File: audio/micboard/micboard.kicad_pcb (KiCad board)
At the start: 2 copper layers, 11 x 7.5 mm, 4 parts, among them P1 CONN_01X04, U1 MIC

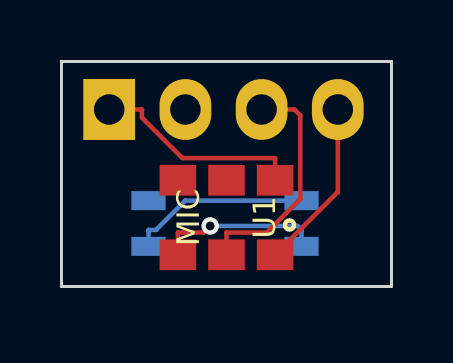
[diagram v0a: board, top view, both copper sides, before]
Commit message: correcting audio board vias
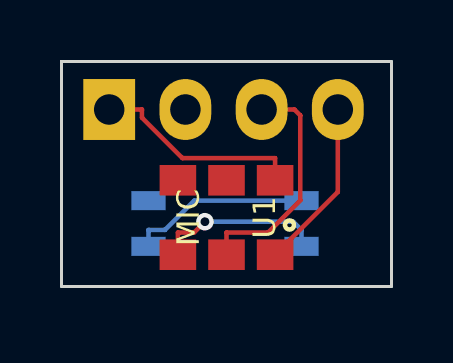
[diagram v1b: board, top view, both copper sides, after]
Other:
- net class Default: via_dia 0.5842 -> 0.635; via_drill 0.3302 -> 0.381
- rule via_min_drill: 0.3302 -> 0.381
- rule via_min_size: 0.5842 -> 0.635
- board text removed: "OUT GN - +"
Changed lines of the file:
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@@
     (links 7)
     (no_connects 0)
-    (area 148.949999 106.949999 160.050001 114.550001)
+    (area 148.007667 106.949999 160.792334 114.550001)
     (thickness 1.6)
-    (drawings 6)
+    (drawings 5)
     (tracks 24)
     (zones 0)
@@
     (segment_width 0.2)
     (edge_width 0.1)
-    (via_size 0.5842)
-    (via_drill 0.3302)
-    (via_min_size 0.5842)
-    (via_min_drill 0.3302)
+    (via_size 0.635)
+    (via_drill 0.381)
+    (via_min_size 0.635)
+    (via_min_drill 0.381)
     (uvia_size 0.508)
     (uvia_drill 0.127)
@@
     (visible_elements FFFFFF7F)
     (pcbplotparams
-      (layerselection 0x00030_80000001)
-      (usegerberextensions false)
+      (layerselection 0x010fc_80000001)
+      (usegerberextensions true)
       (excludeedgelayer true)
       (linewidth 0.100000)
@@
       (psa4output false)
       (plotreference true)
-      (plotvalue true)
+      (plotvalue false)
       (plotinvisibletext false)
       (padsonsilk false)
@@
       (outputformat 1)
       (mirror false)
-      (drillshape 1)
+      (drillshape 0)
       (scaleselection 1)
-      (outputdirectory ""))
+      (outputdirectory gerber/))
   )
   (net 0 "")
@@
     (clearance 0.1524)
     (trace_width 0.1524)
-    (via_dia 0.5842)
-    (via_drill 0.3302)
+    (via_dia 0.635)
+    (via_drill 0.381)
     (uvia_dia 0.508)
     (uvia_drill 0.127)
@@
       (net 3 +5V))
   )
-  (gr_text "OUT GN  -   +" (at 154.6 110.5) (layer B.SilkS)
-    (effects (font (size 0.75 0.75) (thickness 0.1875)) (justify mirror))
-  )
   (gr_line (start 149 114.5) (end 149 107) (angle 90) (layer Edge.Cuts) (width 0.1))
   (gr_line (start 160 114.5) (end 149 114.5) (angle 90) (layer Edge.Cuts) (width 0.1))
@@
   (gr_line (start 149 107) (end 160 107) (angle 90) (layer Edge.Cuts) (width 0.1))
   (gr_line (start 149 107) (end 149 107.1) (angle 90) (layer Edge.Cuts) (width 0.1))
-  (via (at 153.9569 112.4816) (size 0.5842) (layers F.Cu B.Cu) (net 1))
-  (segment (start 153.7374 112.7011) (end 153.9569 112.4816) (width 0.1524) (layer F.Cu) (net 1))
-  (segment (start 152.88 112.7011) (end 153.7374 112.7011) (width 0.1524) (layer F.Cu) (net 1))
-  (segment (start 156.866 112.4816) (end 157 112.6156) (width 0.1524) (layer B.Cu) (net 1))
-  (segment (start 153.9569 112.4816) (end 156.866 112.4816) (width 0.1524) (layer B.Cu) (net 1))
+  (via (at 153.7802 112.3402) (size 0.5842) (layers F.Cu B.Cu) (net 1))
+  (segment (start 153.4193 112.7011) (end 153.7802 112.3402) (width 0.1524) (layer F.Cu) (net 1))
+  (segment (start 152.88 112.7011) (end 153.4193 112.7011) (width 0.1524) (layer F.Cu) (net 1))
+  (segment (start 156.7246 112.3402) (end 157 112.6156) (width 0.1524) (layer B.Cu) (net 1))
+  (segment (start 153.7802 112.3402) (end 156.7246 112.3402) (width 0.1524) (layer B.Cu) (net 1))
   (segment (start 152.88 113.44) (end 152.88 112.7011) (width 0.1524) (layer F.Cu) (net 1))
   (segment (start 157 113.162) (end 157 112.6156) (width 0.1524) (layer B.Cu) (net 1))
-  (segment (start 153.1258 111.638) (end 157 111.638) (width 0.1524) (layer B.Cu) (net 2))
-  (segment (start 152.1482 112.6156) (end 153.1258 111.638) (width 0.1524) (layer B.Cu) (net 2))
-  (segment (start 151.9 112.6156) (end 152.1482 112.6156) (width 0.1524) (layer B.Cu) (net 2))
+  (segment (start 153.424 111.638) (end 157 111.638) (width 0.1524) (layer B.Cu) (net 2))
+  (segment (start 152.4464 112.6156) (end 153.424 111.638) (width 0.1524) (layer B.Cu) (net 2))
+  (segment (start 151.9 112.6156) (end 152.4464 112.6156) (width 0.1524) (layer B.Cu) (net 2))
   (segment (start 151.9 113.162) (end 151.9 112.6156) (width 0.1524) (layer B.Cu) (net 2))
   (segment (start 151.6825 108.8731) (end 151.6825 108.6) (width 0.1524) (layer F.Cu) (net 3))
@@
   (segment (start 156.12 110.96) (end 156.12 110.2211) (width 0.1524) (layer F.Cu) (net 3))
   (segment (start 150.59 108.6) (end 151.6825 108.6) (width 0.1524) (layer F.Cu) (net 3))
-  (segment (start 155.8409 112.7011) (end 154.5 112.7011) (width 0.1524) (layer F.Cu) (net 5))
-  (segment (start 156.959 111.583) (end 155.8409 112.7011) (width 0.1524) (layer F.Cu) (net 5))
-  (segment (start 156.959 108.7965) (end 156.959 111.583) (width 0.1524) (layer F.Cu) (net 5))
-  (segment (start 156.7625 108.6) (end 156.959 108.7965) (width 0.1524) (layer F.Cu) (net 5))
+  (segment (start 156.959 108.7965) (end 156.7625 108.6) (width 0.1524) (layer F.Cu) (net 5))
+  (segment (start 156.959 111.6291) (end 156.959 108.7965) (width 0.1524) (layer F.Cu) (net 5))
+  (segment (start 155.887 112.7011) (end 156.959 111.6291) (width 0.1524) (layer F.Cu) (net 5))
+  (segment (start 154.5 112.7011) (end 155.887 112.7011) (width 0.1524) (layer F.Cu) (net 5))
+  (segment (start 154.5 113.44) (end 154.5 112.7011) (width 0.1524) (layer F.Cu) (net 5))
   (segment (start 155.67 108.6) (end 156.7625 108.6) (width 0.1524) (layer F.Cu) (net 5))
-  (segment (start 154.5 113.44) (end 154.5 112.7011) (width 0.1524) (layer F.Cu) (net 5))
   (segment (start 158.21 111.35) (end 158.21 108.6) (width 0.1524) (layer F.Cu) (net 6))
   (segment (start 156.12 113.44) (end 158.21 111.35) (width 0.1524) (layer F.Cu) (net 6))

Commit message: finalizing audio board
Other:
- board text added: "OUT GN - +"
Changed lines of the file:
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@@
-(kicad_pcb (version 4) (host pcbnew "(2014-09-08 BZR 5123)-product")
+(kicad_pcb (version 4) (host pcbnew "(2014-09-29 BZR 5155)-product")
   (general
     (links 7)
@@
     (area 148.007667 106.949999 160.792334 114.550001)
     (thickness 1.6)
-    (drawings 5)
+    (drawings 6)
     (tracks 24)
     (zones 0)
@@
       (net 3 +5V))
   )
+  (gr_text "OUT  GN  -   +" (at 154.813 110.49) (layer B.Mask)
+    (effects (font (size 0.75 0.75) (thickness 0.1875)) (justify mirror))
+  )
   (gr_line (start 149 114.5) (end 149 107) (angle 90) (layer Edge.Cuts) (width 0.1))
   (gr_line (start 160 114.5) (end 149 114.5) (angle 90) (layer Edge.Cuts) (width 0.1))
@@
   (gr_line (start 149 107) (end 160 107) (angle 90) (layer Edge.Cuts) (width 0.1))
   (gr_line (start 149 107) (end 149 107.1) (angle 90) (layer Edge.Cuts) (width 0.1))
-  (via (at 153.7802 112.3402) (size 0.5842) (layers F.Cu B.Cu) (net 1))
+  (via (at 153.7802 112.3402) (size 0.635) (layers F.Cu B.Cu) (net 1))
   (segment (start 153.4193 112.7011) (end 153.7802 112.3402) (width 0.1524) (layer F.Cu) (net 1))
   (segment (start 152.88 112.7011) (end 153.4193 112.7011) (width 0.1524) (layer F.Cu) (net 1))

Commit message: changed mic. board done...i hope
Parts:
- removed C1: 0.47uF, SMD_Packages:SMD-0603
- removed R1: 4K7, SMD_Packages:SMD-0603
- P1: value CONN_01X04 -> CONN_01X03; footprint Pin_Headers:Pin_Header_Straight_1x04 -> Pin_Headers:Pin_Header_Straight_1x03; moved to F.Cu
- moved U1 0.10 mm to (154.4, 112.3)
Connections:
- P1 pad 3: GAIN -> OUT
- U1 pad 2: GAIN -> GND
- U1 pad 3: Net-(C1-Pad1) -> +5V
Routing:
- net GAIN: track 7.84 -> 0.00 mm
- net Net-(C1-Pad2): track 6.05 -> 0.00 mm
- net Net-(C1-Pad1): track 5.67 -> 0.00 mm, vias 1 -> 0
- net GND: track 0.00 -> 3.68 mm
- net +5V: track 7.10 -> 6.00 mm
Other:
- board size 11 x 7.5 mm -> 9 x 8 mm
- board text added: "+ - OUT"
- board text removed: "OUT GN - +"
